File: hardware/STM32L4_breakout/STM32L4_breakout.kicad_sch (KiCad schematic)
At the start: 68 parts, among them J1 12V IN, J10 GPIO, J11 SPI1, J12 USART1, J13 USART3, J14 UART4, J15 3.3V, J16 5V, J17 12V, J2 SWD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

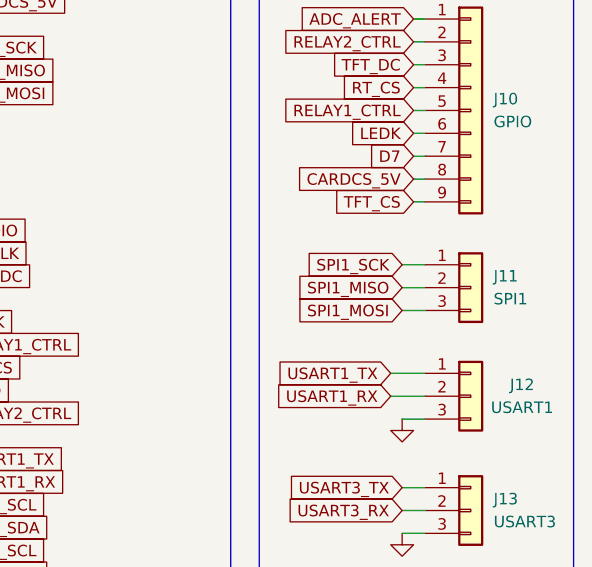
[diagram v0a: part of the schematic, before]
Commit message: breakout board pcb layout WIP
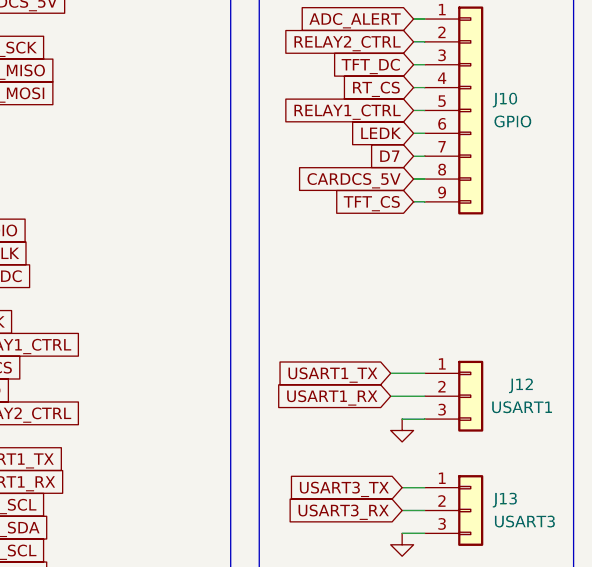
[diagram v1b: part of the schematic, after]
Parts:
- removed J11: SPI1, Connector_PinHeader_2.54mm:PinHeader_1x03_P2.54mm_Vertical, symbol Connector_Generic:Conn_01x03
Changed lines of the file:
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@@
     (stroke (width 0) (type default) (color 0 0 0 0))
   )
-  (wire (pts (xy 262.255 91.44) (xy 264.795 91.44))
-    (stroke (width 0) (type default) (color 0 0 0 0))
-  )
   (wire (pts (xy 31.75 175.895) (xy 43.815 175.895))
     (stroke (width 0) (type default) (color 0 0 0 0))
@@
     (stroke (width 0) (type default) (color 0 0 0 0))
   )
-  (wire (pts (xy 262.255 93.98) (xy 264.795 93.98))
-    (stroke (width 0) (type default) (color 0 0 0 0))
-  )
   (wire (pts (xy 194.31 29.21) (xy 203.2 29.21))
     (stroke (width 0) (type default) (color 0 0 0 0))
@@
     (stroke (width 0) (type default) (color 0 0 0 0))
   )
-  (wire (pts (xy 262.255 88.9) (xy 264.795 88.9))
-    (stroke (width 0) (type default) (color 0 0 0 0))
-  )
   (wire (pts (xy 168.91 123.19) (xy 171.45 123.19))
     (stroke (width 0) (type default) (color 0 0 0 0))
@@
     )
   )
-  (global_label "SPI1_MISO" (shape input) (at 262.255 91.44 180) (fields_autoplaced)
-    (effects (font (size 1.27 1.27)) (justify right))
-    (property "Intersheet References" "${INTERSHEET_REFS}" (id 0) (at 249.9843 91.3606 0)
-      (effects (font (size 1.27 1.27)) (justify right) hide)
-    )
-  )
   (global_label "D7" (shape input) (at 263.525 76.835 180) (fields_autoplaced)
     (effects (font (size 1.27 1.27)) (justify right))
@@
     )
   )
-  (global_label "SPI1_SCK" (shape input) (at 262.255 88.9 180) (fields_autoplaced)
-    (effects (font (size 1.27 1.27)) (justify right))
-    (property "Intersheet References" "${INTERSHEET_REFS}" (id 0) (at 250.8309 88.8206 0)
-      (effects (font (size 1.27 1.27)) (justify right) hide)
-    )
-  )
   (global_label "USART1_TX" (shape input) (at 260.985 100.965 180) (fields_autoplaced)
     (effects (font (size 1.27 1.27)) (justify right))
@@
     )
   )
-  (global_label "SPI1_MOSI" (shape input) (at 262.255 93.98 180) (fields_autoplaced)
-    (effects (font (size 1.27 1.27)) (justify right))
-    (property "Intersheet References" "${INTERSHEET_REFS}" (id 0) (at 249.9843 93.9006 0)
-      (effects (font (size 1.27 1.27)) (justify right) hide)
-    )
-  )
   (global_label "I2C2_SDA" (shape input) (at 212.09 123.19 0) (fields_autoplaced)
     (effects (font (size 1.27 1.27)) (justify left))
@@
     (pin "1")
   )
-  (symbol (lib_id "Connector_Generic:Conn_01x03") (at 269.875 91.44 0) (unit 1)
-    (in_bom yes) (on_board yes) (fields_autoplaced)
-    (property "Reference" "J11" (id 0) (at 272.415 90.1699 0)
-      (effects (font (size 1.27 1.27)) (justify left))
-    )
-    (property "Value" "SPI1" (id 1) (at 272.415 92.7099 0)
-      (effects (font (size 1.27 1.27)) (justify left))
-    )
-    (property "Footprint" "Connector_PinHeader_2.54mm:PinHeader_1x03_P2.54mm_Vertical" (id 2) (at 269.875 91.44 0)
-      (effects (font (size 1.27 1.27)) hide)
-    )
-    (property "Datasheet" "~" (id 3) (at 269.875 91.44 0)
-      (effects (font (size 1.27 1.27)) hide)
-    )
-    (pin "1")
-    (pin "2")
-    (pin "3")
-  )
   (symbol (lib_id "Device:C_Small") (at 38.735 36.195 0) (unit 1)
     (in_bom yes) (on_board yes)
@@
       (reference "J10") (unit 1) (value "GPIO") (footprint "Connector_PinHeader_2.54mm:PinHeader_1x09_P2.54mm_Vertical")
     )
-    (path "/9bf6ec90-fb4d-4ef8-ab83-f53f91b222e0"
-      (reference "J11") (unit 1) (value "SPI1") (footprint "Connector_PinHeader_2.54mm:PinHeader_1x03_P2.54mm_Vertical")
-    )
     (path "/ba332e87-3519-4751-ac8c-5549ca6482ff"

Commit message: breakout board signal routing WIP
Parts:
- removed J14: UART4, Connector_PinHeader_2.54mm:PinHeader_1x03_P2.54mm_Vertical, symbol Connector_Generic:Conn_01x03
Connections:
- net CARDCS_5V: no longer J10.8 (Pin_8)
- net D7: no longer J10.7 (Pin_7)
- net LEDK: no longer J10.6 (Pin_6)
- net RELAY1_CTRL: no longer J6.7 (Pin_7)
- net RELAY2_CTRL: no longer J6.6 (Pin_6)
- net RT_CS: no longer J10.4 (Pin_4)
- net TFT_CS: no longer J10.9 (Pin_9)
- net TFT_DC: no longer J10.3 (Pin_3)
- no-connect marks 30 -> 38
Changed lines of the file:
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@@
   (no_connect (at 168.91 82.55))
   (no_connect (at 168.91 90.17))
+  (no_connect (at 62.865 170.815))
   (no_connect (at 24.13 173.355))
   (no_connect (at 209.55 80.01))
   (no_connect (at 168.91 115.57))
   (no_connect (at 209.55 107.95))
+  (no_connect (at 263.525 69.215))
   (no_connect (at 209.55 128.27))
   (no_connect (at 168.91 113.03))
@@
   (no_connect (at 168.91 120.65))
   (no_connect (at 209.55 74.93))
+  (no_connect (at 263.525 81.915))
+  (no_connect (at 263.525 66.675))
+  (no_connect (at 263.525 79.375))
   (no_connect (at 209.55 130.81))
   (no_connect (at 168.91 123.19))
+  (no_connect (at 263.525 76.835))
   (no_connect (at 168.91 125.73))
   (no_connect (at 24.13 180.975))
+  (no_connect (at 263.525 74.295))
   (no_connect (at 209.55 82.55))
   (no_connect (at 36.195 160.655))
   (no_connect (at 168.91 85.09))
   (no_connect (at 168.91 102.87))
+  (no_connect (at 62.865 173.355))
   (no_connect (at 24.13 175.895))
   (no_connect (at 209.55 133.35))
@@
     (stroke (width 0) (type default) (color 0 0 0 0))
   )
-  (wire (pts (xy 262.255 126.365) (xy 264.795 126.365))
-    (stroke (width 0) (type default) (color 0 0 0 0))
-  )
   (wire (pts (xy 64.135 30.48) (xy 64.135 33.655))
     (stroke (width 0) (type default) (color 0 0 0 0))
@@
     (stroke (width 0) (type default) (color 0 0 0 0))
   )
-  (wire (pts (xy 262.255 131.445) (xy 264.795 131.445))
-    (stroke (width 0) (type default) (color 0 0 0 0))
-  )
   (wire (pts (xy 262.89 41.275) (xy 264.795 41.275))
     (stroke (width 0) (type default) (color 0 0 0 0))
@@
     (stroke (width 0) (type default) (color 0 0 0 0))
   )
-  (wire (pts (xy 62.865 173.355) (xy 66.04 173.355))
-    (stroke (width 0) (type default) (color 0 0 0 0))
-  )
   (wire (pts (xy 50.8 38.1) (xy 50.8 38.735))
     (stroke (width 0) (type default) (color 0 0 0 0))
@@
     (stroke (width 0) (type default) (color 0 0 0 0))
   )
-  (wire (pts (xy 262.255 128.905) (xy 264.795 128.905))
-    (stroke (width 0) (type default) (color 0 0 0 0))
-  )
   (wire (pts (xy 118.745 180.34) (xy 123.825 180.34))
     (stroke (width 0) (type default) (color 0 0 0 0))
@@
     (stroke (width 0) (type default) (color 0 0 0 0))
   )
-  (wire (pts (xy 62.865 170.815) (xy 66.04 170.815))
-    (stroke (width 0) (type default) (color 0 0 0 0))
-  )
   (wire (pts (xy 65.405 150.495) (xy 62.865 150.495))
     (stroke (width 0) (type default) (color 0 0 0 0))
@@
     (effects (font (size 1.27 1.27)) (justify left bottom))
   )
-  (global_label "CARDCS_5V" (shape input) (at 263.525 79.375 180) (fields_autoplaced)
-    (effects (font (size 1.27 1.27)) (justify right))
-    (property "Intersheet References" "${INTERSHEET_REFS}" (id 0) (at 250.4681 79.4544 0)
-      (effects (font (size 1.27 1.27)) (justify right) hide)
-    )
-  )
   (global_label "RELAY1_CTRL" (shape input) (at 263.525 71.755 180) (fields_autoplaced)
     (effects (font (size 1.27 1.27)) (justify right))
@@
     )
   )
-  (global_label "TFT_CS" (shape input) (at 263.525 81.915 180) (fields_autoplaced)
-    (effects (font (size 1.27 1.27)) (justify right))
-    (property "Intersheet References" "${INTERSHEET_REFS}" (id 0) (at 254.6409 81.8356 0)
-      (effects (font (size 1.27 1.27)) (justify right) hide)
-    )
-  )
   (global_label "STM_NRST" (shape input) (at 97.79 99.695 0) (fields_autoplaced)
     (effects (font (size 1.27 1.27)) (justify left))
@@
     )
   )
-  (global_label "RT_CS" (shape input) (at 263.525 69.215 180) (fields_autoplaced)
-    (effects (font (size 1.27 1.27)) (justify right))
-    (property "Intersheet References" "${INTERSHEET_REFS}" (id 0) (at 255.4271 69.1356 0)
-      (effects (font (size 1.27 1.27)) (justify right) hide)
-    )
-  )
   (global_label "CARDCS_5V" (shape input) (at 66.04 175.895 0) (fields_autoplaced)
     (effects (font (size 1.27 1.27)) (justify left))
@@
     )
   )
-  (global_label "D7" (shape input) (at 263.525 76.835 180) (fields_autoplaced)
-    (effects (font (size 1.27 1.27)) (justify right))
-    (property "Intersheet References" "${INTERSHEET_REFS}" (id 0) (at 258.6324 76.7556 0)
-      (effects (font (size 1.27 1.27)) (justify right) hide)
-    )
-  )
   (global_label "RT_CS" (shape input) (at 65.405 160.655 0) (fields_autoplaced)
     (effects (font (size 1.27 1.27)) (justify left))
@@
     )
   )
-  (global_label "RELAY2_CTRL" (shape input) (at 66.04 173.355 0) (fields_autoplaced)
-    (effects (font (size 1.27 1.27)) (justify left))
-    (property "Intersheet References" "${INTERSHEET_REFS}" (id 0) (at 80.7902 173.2756 0)
-      (effects (font (size 1.27 1.27)) (justify left) hide)
-    )
-  )
   (global_label "I2C3_SCL" (shape input) (at 262.89 48.26 180) (fields_autoplaced)
     (effects (font (size 1.27 1.27)) (justify right))
@@
     )
   )
-  (global_label "UART4_TX" (shape input) (at 262.255 126.365 180) (fields_autoplaced)
-    (effects (font (size 1.27 1.27)) (justify right))
-    (property "Intersheet References" "${INTERSHEET_REFS}" (id 0) (at 250.8309 126.2856 0)
-      (effects (font (size 1.27 1.27)) (justify right) hide)
-    )
-  )
   (global_label "SPI1_MOSI" (shape input) (at 65.405 153.035 0) (fields_autoplaced)
     (effects (font (size 1.27 1.27)) (justify left))
@@
     )
   )
-  (global_label "RELAY1_CTRL" (shape input) (at 66.04 170.815 0) (fields_autoplaced)
-    (effects (font (size 1.27 1.27)) (justify left))
-    (property "Intersheet References" "${INTERSHEET_REFS}" (id 0) (at 80.7902 170.7356 0)
-      (effects (font (size 1.27 1.27)) (justify left) hide)
-    )
-  )
   (global_label "USART1_RX" (shape input) (at 212.09 113.03 0) (fields_autoplaced)
     (effects (font (size 1.27 1.27)) (justify left))
@@
     )
   )
-  (global_label "UART4_RX" (shape input) (at 262.255 128.905 180) (fields_autoplaced)
-    (effects (font (size 1.27 1.27)) (justify right))
-    (property "Intersheet References" "${INTERSHEET_REFS}" (id 0) (at 250.5286 128.8256 0)
-      (effects (font (size 1.27 1.27)) (justify right) hide)
-    )
-  )
   (global_label "SPI1_SCK" (shape input) (at 212.09 64.77 0) (fields_autoplaced)
     (effects (font (size 1.27 1.27)) (justify left))
@@
     )
   )
-  (global_label "TFT_DC" (shape input) (at 263.525 66.675 180) (fields_autoplaced)
-    (effects (font (size 1.27 1.27)) (justify right))
-    (property "Intersheet References" "${INTERSHEET_REFS}" (id 0) (at 254.5805 66.5956 0)
-      (effects (font (size 1.27 1.27)) (justify right) hide)
-    )
-  )
   (global_label "OSC32IN" (shape input) (at 166.37 130.81 180) (fields_autoplaced)
     (effects (font (size 1.27 1.27)) (justify right))
@@
     )
   )
-  (global_label "LEDK" (shape input) (at 263.525 74.295 180) (fields_autoplaced)
-    (effects (font (size 1.27 1.27)) (justify right))
-    (property "Intersheet References" "${INTERSHEET_REFS}" (id 0) (at 256.3948 74.2156 0)
-      (effects (font (size 1.27 1.27)) (justify right) hide)
-    )
-  )
   (global_label "I2C1_SDA" (shape input) (at 59.055 109.22 0) (fields_autoplaced)
     (effects (font (size 1.27 1.27)) (justify left))
@@
     (pin "2")
   )
-  (symbol (lib_id "power:GND") (at 262.255 131.445 0) (unit 1)
-    (in_bom yes) (on_board yes) (fields_autoplaced)
-    (property "Reference" "#PWR043" (id 0) (at 262.255 137.795 0)
-      (effects (font (size 1.27 1.27)) hide)
-    )
-    (property "Value" "GND" (id 1) (at 262.255 136.525 0)
-      (effects (font (size 1.27 1.27)) hide)
-    )
-    (property "Footprint" "" (id 2) (at 262.255 131.445 0)
-      (effects (font (size 1.27 1.27)) hide)
-    )
-    (property "Datasheet" "" (id 3) (at 262.255 131.445 0)
-      (effects (font (size 1.27 1.27)) hide)
-    )
-    (pin "1")
-  )
   (symbol (lib_id "power:PWR_FLAG") (at 213.36 27.94 0) (unit 1)
     (in_bom yes) (on_board yes) (fields_autoplaced)
@@
     (pin "1")
   )
-  (symbol (lib_id "Connector_Generic:Conn_01x03") (at 269.875 128.905 0) (unit 1)
-    (in_bom yes) (on_board yes)
-    (property "Reference" "J14" (id 0) (at 272.415 127.6349 0)
-      (effects (font (size 1.27 1.27)) (justify left))
-    )
-    (property "Value" "UART4" (id 1) (at 272.415 130.1749 0)
-      (effects (font (size 1.27 1.27)) (justify left))
-    )
-    (property "Footprint" "Connector_PinHeader_2.54mm:PinHeader_1x03_P2.54mm_Vertical" (id 2) (at 269.875 128.905 0)
-      (effects (font (size 1.27 1.27)) hide)
-    )
-    (property "Datasheet" "~" (id 3) (at 269.875 128.905 0)
-      (effects (font (size 1.27 1.27)) hide)
-    )
-    (pin "1")
-    (pin "2")
-    (pin "3")
-  )
   (symbol (lib_id "power:+3.3V") (at 55.245 95.25 0) (unit 1)
     (in_bom yes) (on_board yes)
@@
       (reference "#PWR042") (unit 1) (value "GND") (footprint "")
     )
-    (path "/4a8094da-141b-4e22-9942-80faa75cb312"
-      (reference "#PWR043") (unit 1) (value "GND") (footprint "")
-    )
     (path "/5faa3663-1cde-4241-a4ce-4f79e7fbfe0a"
       (reference "#PWR044") (unit 1) (value "GND") (footprint "")
@@
       (reference "J13") (unit 1) (value "USART3") (footprint "Connector_PinHeader_2.54mm:PinHeader_1x03_P2.54mm_Vertical")
     )
-    (path "/70b380d3-3856-4255-af62-fd9df70ff722"
-      (reference "J14") (unit 1) (value "UART4") (footprint "Connector_PinHeader_2.54mm:PinHeader_1x03_P2.54mm_Vertical")
-    )
     (path "/ea8310bc-b60d-4fa4-a884-85caa2804f75"
